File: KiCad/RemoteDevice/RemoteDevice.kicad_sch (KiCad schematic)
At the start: 42 parts, among them J1 Alim, J2 CN1, Q1 Si4435, SW1 BP, SW2 BP, U1 XC9140, U2 STM32L041F6Px, U3 MCP6281, U4 ADT7410TRZ, U5 MCP6281, U6 RT606, U7 Microphone

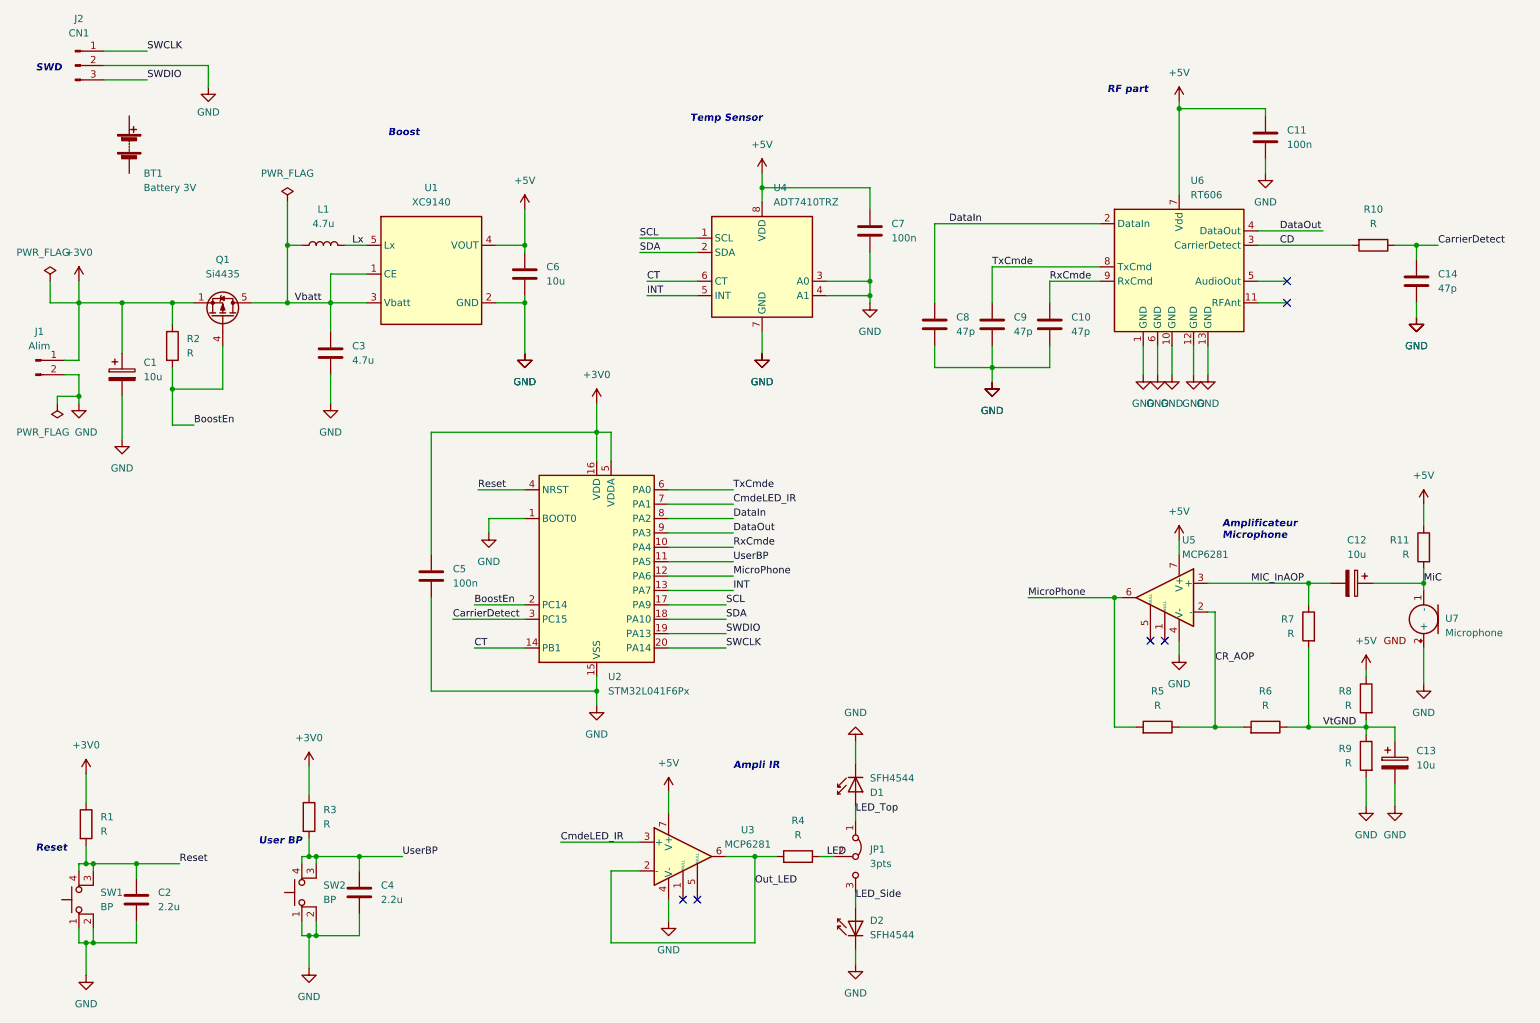
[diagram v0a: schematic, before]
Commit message: Version béta, production josé GEI, ajout d'une résistance série sur le micro pour ne pas griller l'IO (5V max)
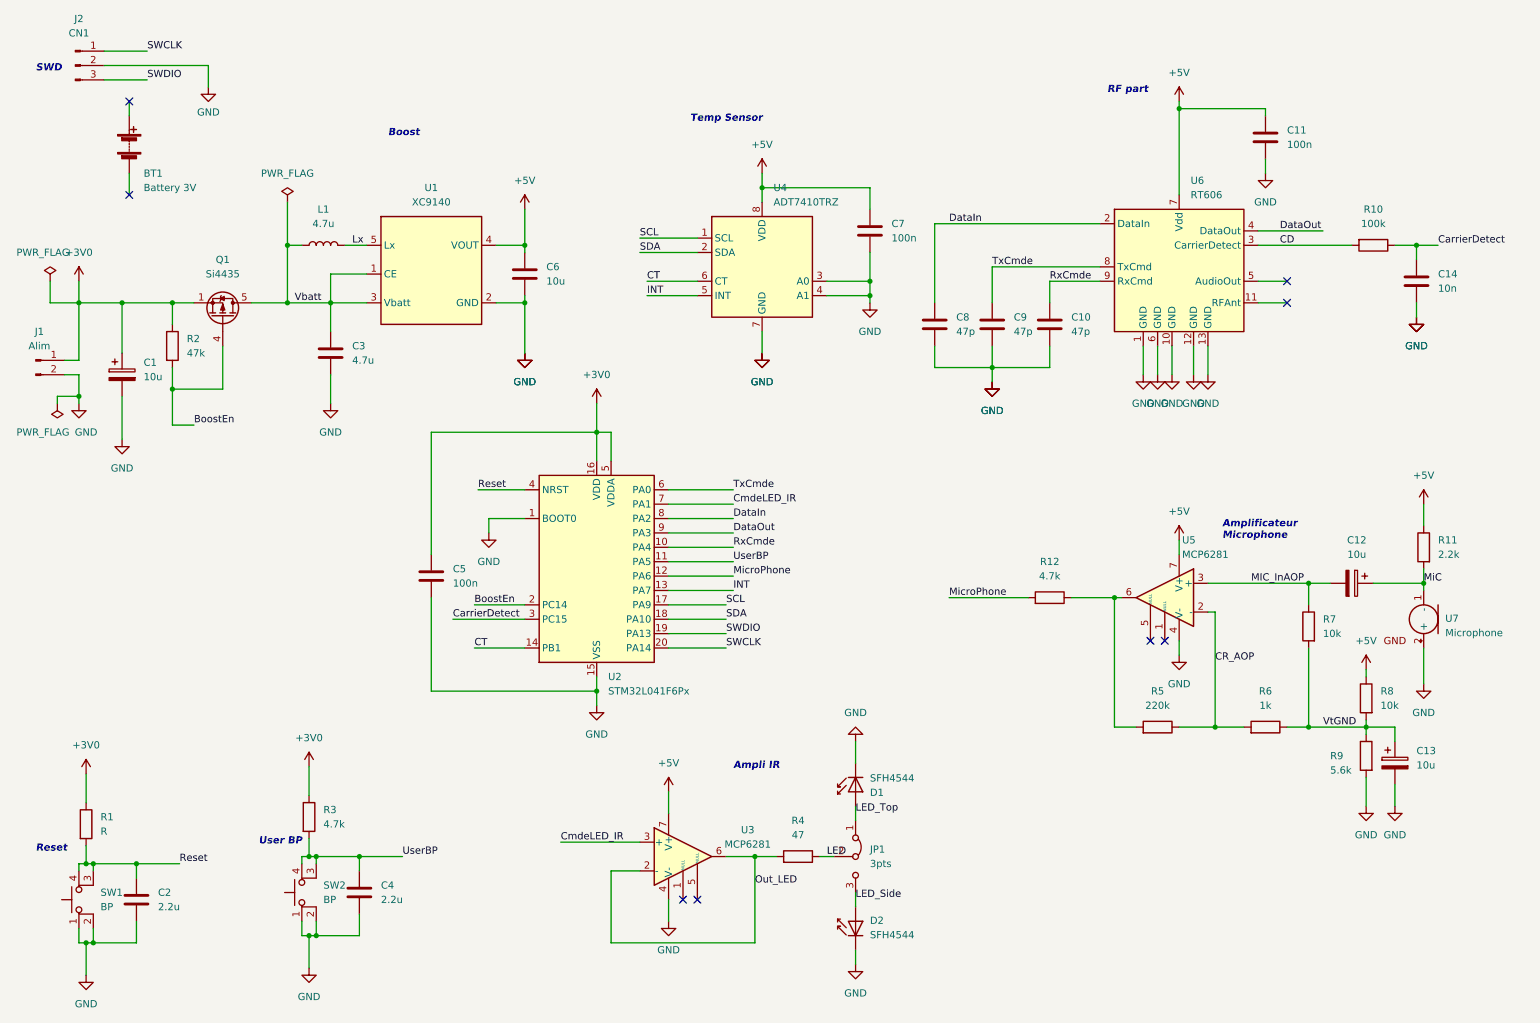
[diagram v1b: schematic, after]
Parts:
- added R12: 4.7k, Resistor_SMD:R_1206_3216Metric, symbol Device:R
- C14: value 47p -> 10n; footprint Capacitor_SMD:C_0805_2012Metric -> Capacitor_SMD:C_1206_3216Metric
- R10: value R -> 100k
- R11: value R -> 2.2k
- R2: value R -> 47k
- R3: value R -> 4.7k
- R4: value R -> 47
- R5: value R -> 220k
- R6: value R -> 1k
- R7, R8: value R -> 10k
- R9: value R -> 5.6k
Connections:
- net MicroPhone: now also R12.2; no longer R5.2, U5.6
- new net: R12.1, R5.2, U5.6
- no-connect marks 6 -> 8
